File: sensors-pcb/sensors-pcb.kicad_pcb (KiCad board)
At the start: 2 copper layers, 75 x 55 mm, 67 parts, among them J1 Network Connector, J2 STDC14, J3 Conn_Coaxial, SW1 SW_Push, U1 MAX-M8Q, U2 BNO055, U3 LD39050PU33R, U4 STM32G474RBT6, U5 SN65HVD230, Y1 32kHz, Y2 8MHz

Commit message: sensors-pcb: set TPs solder junctions as DNP
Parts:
- R5: value 40.2k -> 39k
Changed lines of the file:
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@@
 		(sheetname "/")
 		(sheetfile "sensors-pcb.kicad_sch")
-		(attr through_hole)
+		(attr through_hole dnp)
 		(fp_circle
 			(center 0 0)
@@
 		(sheetname "/")
 		(sheetfile "sensors-pcb.kicad_sch")
-		(attr through_hole)
+		(attr through_hole dnp)
 		(fp_circle
 			(center 0 0)
@@
 		(sheetname "/")
 		(sheetfile "sensors-pcb.kicad_sch")
-		(attr through_hole)
+		(attr through_hole dnp)
 		(fp_circle
 			(center 0 0)
@@
 		(sheetfile "sensors-pcb.kicad_sch")
 		(zone_connect 1)
-		(attr exclude_from_pos_files exclude_from_bom allow_soldermask_bridges)
+		(attr exclude_from_pos_files exclude_from_bom dnp allow_soldermask_bridges)
 		(fp_rect
 			(start -0.15 -0.75)
@@
 		(sheetname "/")
 		(sheetfile "sensors-pcb.kicad_sch")
-		(attr through_hole)
+		(attr through_hole dnp)
 		(fp_circle
 			(center 0 0)
@@
 		(sheetname "/")
 		(sheetfile "sensors-pcb.kicad_sch")
-		(attr through_hole)
+		(attr through_hole dnp)
 		(fp_circle
 			(center 0 0)
@@
 			)
 		)
-		(property "Value" "40.2k"
+		(property "Value" "39k"
 			(at 0 0 135)
 			(layer "F.Fab")
@@
 			)
 		)
-		(property "JLCPCB" "C25893"
+		(property "JLCPCB" "C25783"
 			(at 0 0 135)
 			(unlocked yes)
@@
 		(sheetname "/")
 		(sheetfile "sensors-pcb.kicad_sch")
-		(attr through_hole)
+		(attr through_hole dnp)
 		(fp_circle
 			(center 0 0)
@@
 		(sheetfile "sensors-pcb.kicad_sch")
 		(zone_connect 1)
-		(attr exclude_from_pos_files exclude_from_bom allow_soldermask_bridges)
+		(attr exclude_from_pos_files exclude_from_bom dnp allow_soldermask_bridges)
 		(fp_rect
 			(start -0.15 -0.75)
@@
 		(sheetname "/")
 		(sheetfile "sensors-pcb.kicad_sch")
-		(attr through_hole)
+		(attr through_hole dnp)
 		(fp_circle
 			(center 0 0)

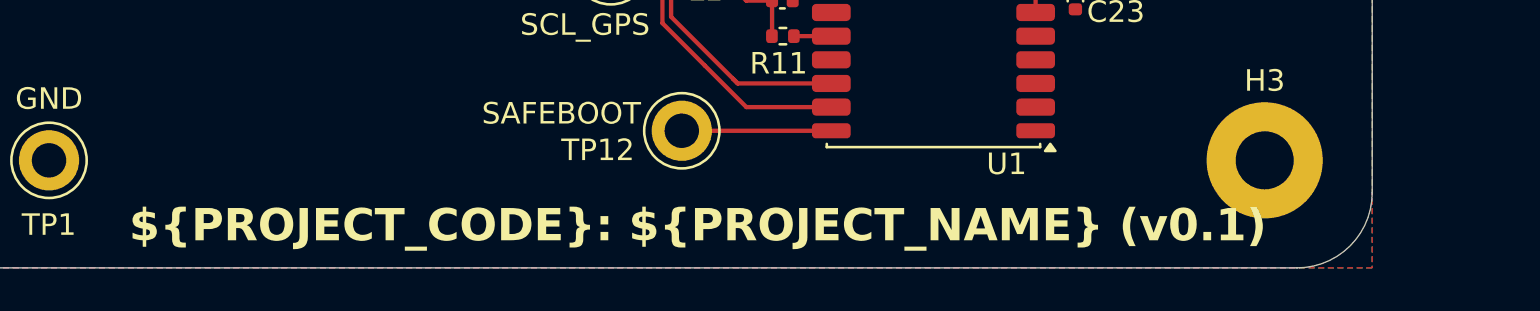
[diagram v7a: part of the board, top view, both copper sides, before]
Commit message: sensors-pcb: update PCB metadata and info block
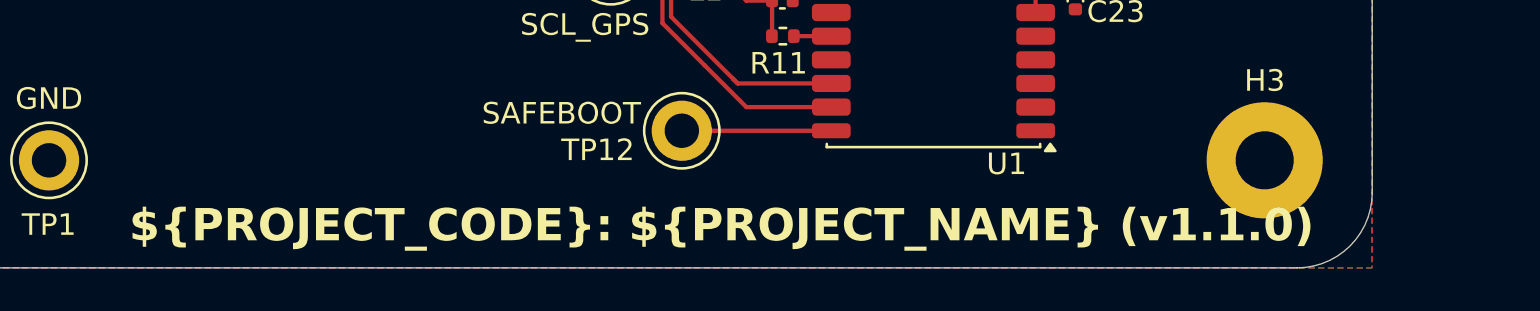
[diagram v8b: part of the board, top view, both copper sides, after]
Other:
- board text added: "${PROJECT_CODE}: ${PROJECT_NAME} (${REVISION})"
- board text removed: "${PROJECT_CODE}: ${PROJECT_NAME} (v0.1)"
- board text removed: "${REFERENCE}"
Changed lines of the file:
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@@
 	(title_block
 		(title "Base board layout")
-		(date "2025-04-06")
-		(rev "v1.0.0")
+		(date "2026-03-16")
+		(rev "v1.1.0")
 	)
 	(layers
@@
 		)
 	)
-	(property "AUTHOR" "Malakham Pravongviengkham, Karima Rahmoun, Romain Stryckman")
+	(property "AUTHOR" "Malakham P., Karima R. et Romain S.")
 	(property "CONTRIBUTORS" "")
 	(property "PROJECT_CODE" "PCB.05")
 	(property "PROJECT_NAME" "Sensors PCB")
-	(property "REVIEWERS" "Eliot Fondère")
+	(property "REVIEWERS" "Eliot F.")
 	(net 0 "")
 	(net 1 "GND")
@@
 		(layer "Edge.Cuts")
 	)
-	(gr_text "${PROJECT_CODE}: ${PROJECT_NAME} (v0.1)"
+	(gr_text "${PROJECT_CODE}: ${PROJECT_NAME} (${REVISION})"
 		(at 207.2 75.4 0)
 		(layer "F.SilkS")
@@
 		)
 	)
-	(gr_text "${REFERENCE}"
-		(at 235.33 36.36 0)
-		(layer "F.Fab")
-		(effects
-			(font
-				(size 0.25 0.25)
-				(thickness 0.04)
-			)
-		)
-	)
